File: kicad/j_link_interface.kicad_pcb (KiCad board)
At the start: 4 copper layers, 22.5 x 26.2 mm, 9 parts, among them J1 Conn_01x05_Pin, J2 SSW-110-02-G-D-RA-N, J3 FTSH-107-01-X-DV-K

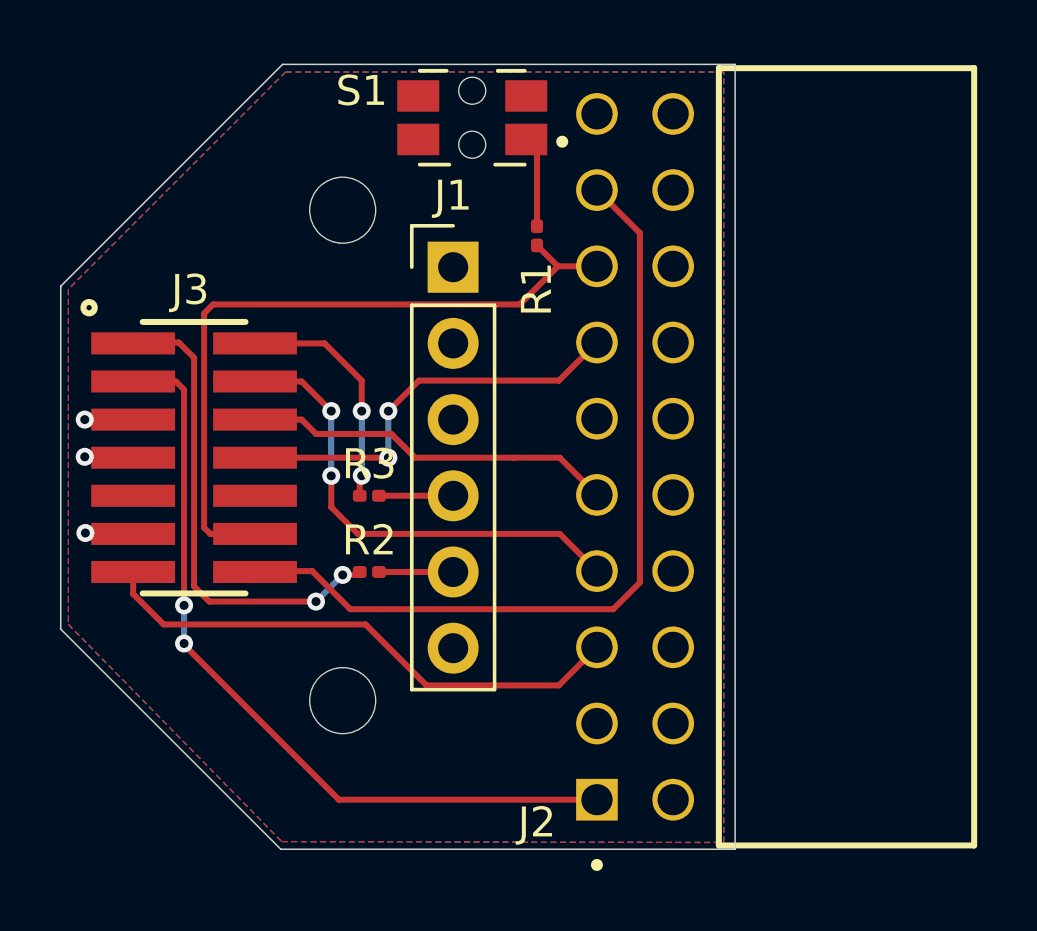
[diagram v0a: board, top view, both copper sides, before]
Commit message: Swapped Tx/Rx labels for clarity as they were related to the UARTs on the target board. Some minor updates to traces.
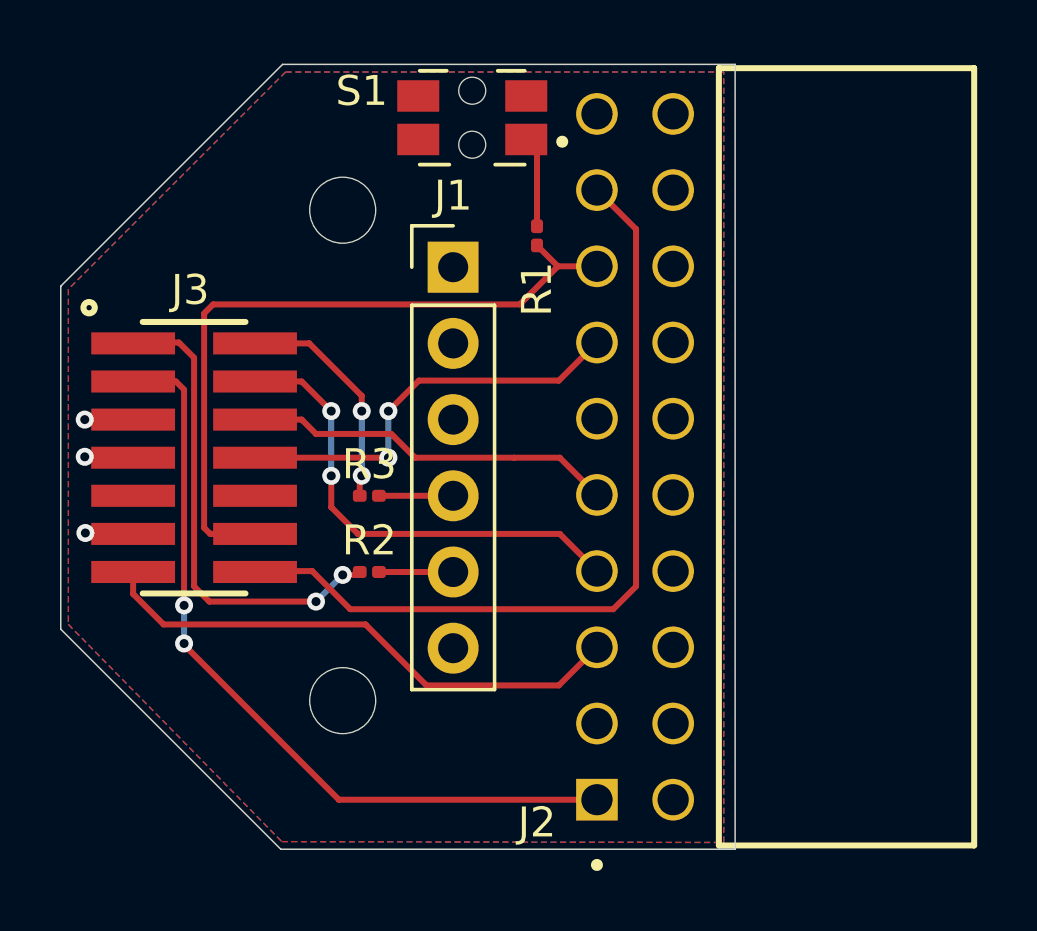
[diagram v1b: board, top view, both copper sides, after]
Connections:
- J2 pad 17: /VCP_TX -> /VCP_RX
- J2 pad 5: /VCP_RX -> /VCP_TX
- J3 pad 1: /FTD_TX -> /FTD_RX
- J3 pad 13: /VCP_RX -> /VCP_TX
- J3 pad 14: /VCP_TX -> /VCP_RX
- J3 pad 2: /FTD_RX -> /FTD_TX
- R2 pad 1: /FTD_TX -> /FTD_RX
- R3 pad 1: /FTD_RX -> /FTD_TX
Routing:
- net /VCP_TX: track 27.4 -> 18.0 mm
- net /VCP_RX: track 18.0 -> 27.3 mm
- net /FTD_TX: track 16.2 -> 7.64 mm
- net /FTD_RX: track 7.94 -> 16.2 mm
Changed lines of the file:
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@@
 			(layers "F.Cu" "F.Mask")
 			(roundrect_rratio 0.25)
-			(net 27 "/FTD_TX")
+			(net 26 "/FTD_RX")
 			(pintype "passive")
 		)
@@
 			(layers "F.Cu" "F.Mask")
 			(roundrect_rratio 0.25)
-			(net 26 "/FTD_RX")
+			(net 27 "/FTD_TX")
 			(pintype "passive")
 		)
@@
 			(layers "*.Cu" "*.Mask")
 			(remove_unused_layers no)
-			(net 3 "/VCP_RX")
+			(net 8 "/VCP_TX")
 			(pinfunction "Pin_5")
 			(pintype "passive")
@@
 			(layers "*.Cu" "*.Mask")
 			(remove_unused_layers no)
-			(net 8 "/VCP_TX")
+			(net 3 "/VCP_RX")
 			(pinfunction "Pin_17")
 			(pintype "passive")
@@
 			(size 0.7366 2.794)
 			(layers "F.Cu" "F.Mask" "F.Paste")
-			(net 27 "/FTD_TX")
+			(net 26 "/FTD_RX")
 			(pinfunction "Pin_1")
 			(pintype "passive")
@@
 			(size 0.7366 2.794)
 			(layers "F.Cu" "F.Mask" "F.Paste")
-			(net 26 "/FTD_RX")
+			(net 27 "/FTD_TX")
 			(pinfunction "Pin_2")
 			(pintype "passive")
@@
 			(size 0.7366 2.794)
 			(layers "F.Cu" "F.Mask" "F.Paste")
-			(net 3 "/VCP_RX")
+			(net 8 "/VCP_TX")
 			(pinfunction "Pin_13")
 			(pintype "passive")
@@
 			(size 0.7366 2.794)
 			(layers "F.Cu" "F.Mask" "F.Paste")
-			(net 8 "/VCP_TX")
+			(net 3 "/VCP_RX")
 			(pinfunction "Pin_14")
 			(pintype "passive")
@@
 	)
 	(segment
-		(start 108.839 80.137)
-		(end 109.855 81.153)
+		(start 125.603 79.883)
+		(end 124.841 80.645)
 		(width 0.2)
 		(layer "F.Cu")
@@
 	)
 	(segment
-		(start 116.586 81.153)
-		(end 118.618 83.185)
+		(start 124.841 80.645)
+		(end 116.078 80.645)
 		(width 0.2)
 		(layer "F.Cu")
@@
 	)
 	(segment
-		(start 109.855 81.153)
-		(end 116.586 81.153)
+		(start 112.9325 79.375)
+		(end 112.903 79.4045)
 		(width 0.2)
 		(layer "F.Cu")
@@
 	)
 	(segment
-		(start 118.618 83.185)
-		(end 123.0295 83.185)
+		(start 116.078 80.645)
+		(end 114.808 79.375)
 		(width 0.2)
 		(layer "F.Cu")
@@
 	)
 	(segment
-		(start 108.839 79.4045)
-		(end 108.839 80.137)
+		(start 114.808 79.375)
+		(end 112.9325 79.375)
 		(width 0.2)
 		(layer "F.Cu")
@@
 	)
 	(segment
-		(start 123.0295 83.185)
-		(end 124.2995 81.915)
+		(start 124.2995 66.675)
+		(end 125.603 67.9785)
+		(width 0.2)
+		(layer "F.Cu")
+		(net 3)
+	)
+	(segment
+		(start 125.603 67.9785)
+		(end 125.603 79.883)
 		(width 0.2)
 		(layer "F.Cu")
@@
 	)
 	(segment
-		(start 124.841 80.645)
-		(end 116.078 80.645)
-		(width 0.2)
-		(layer "F.Cu")
-		(net 8)
-	)
-	(segment
-		(start 116.078 80.645)
-		(end 114.808 79.375)
+		(start 108.839 80.137)
+		(end 109.855 81.153)
 		(width 0.2)
 		(layer "F.Cu")
@@
 	)
 	(segment
-		(start 125.73 68.1055)
-		(end 125.73 79.756)
+		(start 116.586 81.153)
+		(end 118.618 83.185)
 		(width 0.2)
 		(layer "F.Cu")
@@
 	)
 	(segment
-		(start 114.808 79.375)
-		(end 112.9325 79.375)
+		(start 109.855 81.153)
+		(end 116.586 81.153)
 		(width 0.2)
 		(layer "F.Cu")
@@
 	)
 	(segment
-		(start 112.9325 79.375)
-		(end 112.903 79.4045)
+		(start 118.618 83.185)
+		(end 123.0295 83.185)
 		(width 0.2)
 		(layer "F.Cu")
@@
 	)
 	(segment
-		(start 125.73 79.756)
-		(end 124.841 80.645)
+		(start 108.839 79.4045)
+		(end 108.839 80.137)
 		(width 0.2)
 		(layer "F.Cu")
@@
 	)
 	(segment
-		(start 124.2995 66.675)
-		(end 125.73 68.1055)
+		(start 123.0295 83.185)
+		(end 124.2995 81.915)
 		(width 0.2)
 		(layer "F.Cu")
@@
 	)
 	(segment
-		(start 115.2185 71.7845)
-		(end 112.903 71.7845)
+		(start 110.363 71.755)
+		(end 108.8685 71.755)
 		(width 0.2)
 		(layer "F.Cu")
@@
 	)
 	(segment
-		(start 116.459 76.1945)
-		(end 116.393 76.2605)
+		(start 111.379 80.391)
+		(end 110.871 79.883)
 		(width 0.2)
 		(layer "F.Cu")
@@
 	)
 	(segment
-		(start 116.393 76.2605)
-		(end 116.393 76.8645)
+		(start 108.966 71.6575)
+		(end 108.839 71.7845)
 		(width 0.2)
 		(layer "F.Cu")
@@
 	)
 	(segment
-		(start 116.459 73.025)
-		(end 115.2185 71.7845)
+		(start 115.824 79.502)
+		(end 116.2955 79.502)
 		(width 0.2)
 		(layer "F.Cu")
@@
 	)
 	(segment
-		(start 116.459 74.041)
-		(end 116.459 73.025)
+		(start 110.871 72.263)
+		(end 110.363 71.755)
 		(width 0.2)
 		(layer "F.Cu")
 		(net 26)
 	)
-	(via
-		(at 116.459 76.1945)
-		(size 0.6)
-		(drill 0.3)
-		(layers "F.Cu" "B.Cu")
-		(net 26)
-	)
-	(via
-		(at 116.459 74.041)
-		(size 0.6)
-		(drill 0.3)
-		(layers "F.Cu" "B.Cu")
-		(net 26)
-	)
 	(segment
-		(start 116.459 76.1945)
-		(end 116.459 74.041)
+		(start 110.871 79.883)
+		(end 110.871 72.263)
 		(width 0.2)
-		(layer "B.Cu")
+		(layer "F.Cu")
 		(net 26)
 	)
 	(segment
-		(start 110.363 71.755)
-		(end 108.8685 71.755)
+		(start 114.935 80.391)
+		(end 111.379 80.391)
 		(width 0.2)
 		(layer "F.Cu")
-		(net 27)
+		(net 26)
 	)
 	(segment
-		(start 111.379 80.391)
-		(end 110.871 79.883)
+		(start 116.2955 79.502)
+		(end 116.393 79.4045)
 		(width 0.2)
 		(layer "F.Cu")
-		(net 27)
+		(net 26)
 	)
 	(segment
-		(start 108.966 71.6575)
+		(start 108.8685 71.755)
 		(end 108.839 71.7845)
 		(width 0.2)
 		(layer "F.Cu")
-		(net 27)
+		(net 26)
+	)
+	(via
+		(at 115.824 79.502)
+		(size 0.6)
+		(drill 0.3)
+		(layers "F.Cu" "B.Cu")
+		(net 26)
+	)
+	(via
+		(at 114.935 80.391)
+		(size 0.6)
+		(drill 0.3)
+		(layers "F.Cu" "B.Cu")
+		(net 26)
 	)
 	(segment
-		(start 115.824 79.502)
-		(end 116.2955 79.502)
+		(start 114.935 80.391)
+		(end 115.824 79.502)
 		(width 0.2)
-		(layer "F.Cu")
-		(net 27)
+		(layer "B.Cu")
+		(net 26)
 	)
 	(segment
-		(start 110.871 72.263)
-		(end 110.363 71.755)
+		(start 116.459 76.1945)
+		(end 116.393 76.2605)
 		(width 0.2)
 		(layer "F.Cu")
@@
 	)
 	(segment
-		(start 110.871 79.883)
-		(end 110.871 72.263)
+		(start 116.393 76.2605)
+		(end 116.393 76.8645)
 		(width 0.2)
 		(layer "F.Cu")
@@
 	)
 	(segment
-		(start 114.935 80.391)
-		(end 111.379 80.391)
+		(start 116.459 74.041)
+		(end 116.459 73.533)
 		(width 0.2)
 		(layer "F.Cu")
@@
 	)
 	(segment
-		(start 116.2955 79.502)
-		(end 116.393 79.4045)
+		(start 116.459 73.533)
+		(end 114.7105 71.7845)
 		(width 0.2)
 		(layer "F.Cu")
@@
 	)
 	(segment
-		(start 108.8685 71.755)
-		(end 108.839 71.7845)
+		(start 114.7105 71.7845)
+		(end 112.903 71.7845)
 		(width 0.2)
 		(layer "F.Cu")
@@
 	)
 	(via
-		(at 115.824 79.502)
+		(at 116.459 76.1945)
 		(size 0.6)
 		(drill 0.3)
@@
 	)
 	(via
-		(at 114.935 80.391)
+		(at 116.459 74.041)
 		(size 0.6)
 		(drill 0.3)
@@
 	)
 	(segment
-		(start 114.935 80.391)
-		(end 115.824 79.502)
+		(start 116.459 76.1945)
+		(end 116.459 74.041)
 		(width 0.2)
 		(layer "B.Cu")
